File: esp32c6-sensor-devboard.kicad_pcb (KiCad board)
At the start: 4 copper layers, 90 x 50 mm, 193 parts, among them J1 Conn_01x04_Pin, J2 Micro_SD_Card_Det1, J3 Screw_Terminal_01x02, J4 USB_C_Receptacle_USB2.0_14P, J5 Screw_Terminal_01x02, J6 Screw_Terminal_01x06, J7 Screw_Terminal_01x04, J8 Conn_01x04_Pin, J9 Conn_01x03_Pin, SW1 SW_Push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

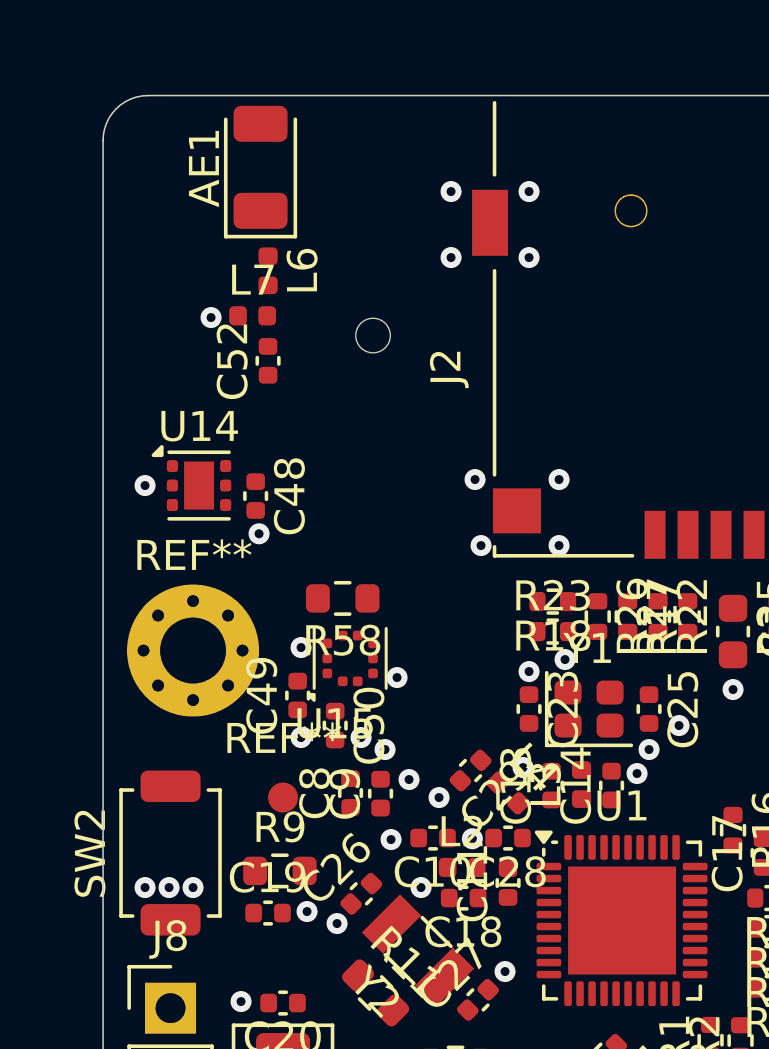
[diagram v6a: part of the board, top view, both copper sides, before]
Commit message: pcb: add rf routing
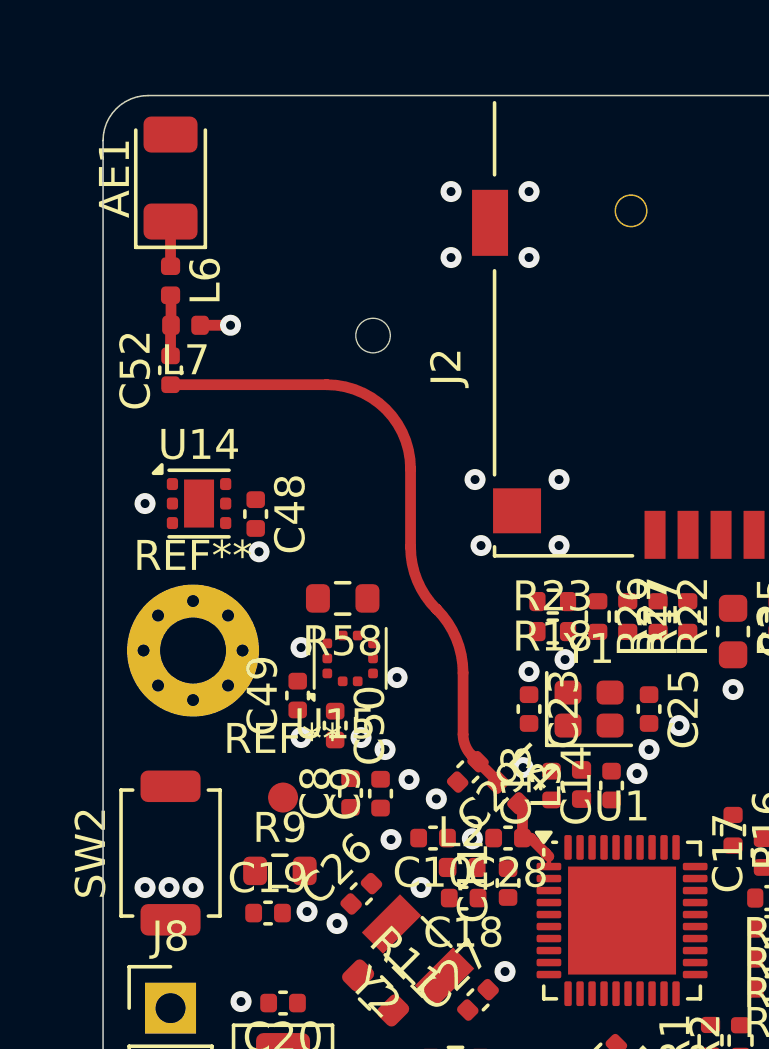
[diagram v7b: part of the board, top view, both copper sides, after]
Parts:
- moved L6 3.27 mm to (134.2, 73.2)
- moved C52 3.27 mm to (134.2, 76.2)
- moved AE1 3.02 mm to (134.2, 69.8)
- moved L7 2.26 mm to (134.8, 74.7), turned to 180 degrees
- moved C48 0.60 mm to (137.1, 81.0)
- moved U14 0.60 mm to (135.2, 80.6)
- moved C29 0.10 mm to (144.2, 89.5)
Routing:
- net /RF_TRANS: track 0.00 -> 20.8 mm
- net /RF_ESP: track 0.00 -> 2.69 mm
- net Net-(C52-Pad2): track 0.00 -> 2.03 mm
- net /RF_ANT: track 0.00 -> 1.49 mm
- net GND: track 0.00 -> 1.01 mm
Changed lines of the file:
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@@
 	(footprint "Capacitor_SMD:C_0402_1005Metric"
 		(layer "F.Cu")
-		(at 144.25 89.5 -135)
+		(at 144.159791 89.544847 -135)
 		(descr "Capacitor SMD 0402 (1005 Metric), square (rectangular) end terminal, IPC-7351 nominal, (Body size source: IPC-SM-782 page 76, https://www.pcb-3d.com/wordpress/wp-content/uploads/ipc-sm-782a_amendment_1_and_2.pdf), generated with kicad-footprint-generator")
 		(tags "capacitor")
@@
 	(footprint "Inductor_SMD:L_0402_1005Metric"
 		(layer "F.Cu")
-		(at 136.985 74.3425)
+		(at 134.75 74.6575 180)
 		(descr "Inductor SMD 0402 (1005 Metric), square (rectangular) end terminal, IPC-7351 nominal, (Body size source: http://www.tortai-tech.com/upload/download/2011102023233369053.pdf), generated with kicad-footprint-generator")
 		(tags "inductor")
@@
 		)
 		(property "JLCPCB Part #" "C77108"
-			(at 0 0 0)
+			(at 0 0 180)
 			(unlocked yes)
 			(layer "F.Fab")
@@
 		)
 		(property "Manufacturer" "Murata"
-			(at 0 0 0)
+			(at 0 0 180)
 			(unlocked yes)
 			(layer "F.Fab")
@@
 		)
 		(property "Manufacturer Part Number" "LQG15HS2N7S02D"
-			(at 0 0 0)
+			(at 0 0 180)
 			(unlocked yes)
 			(layer "F.Fab")
@@
 		(attr smd)
 		(fp_line
-			(start -0.93 -0.47)
-			(end 0.93 -0.47)
+			(start 0.93 0.47)
+			(end -0.93 0.47)
 			(stroke
 				(width 0.05)
@@
 		)
 		(fp_line
-			(start -0.93 0.47)
-			(end -0.93 -0.47)
+			(start 0.93 -0.47)
+			(end 0.93 0.47)
 			(stroke
 				(width 0.05)
@@
 		)
 		(fp_line
-			(start 0.93 -0.47)
-			(end 0.93 0.47)
+			(start -0.93 0.47)
+			(end -0.93 -0.47)
 			(stroke
 				(width 0.05)
@@
 		)
 		(fp_line
-			(start 0.93 0.47)
-			(end -0.93 0.47)
+			(start -0.93 -0.47)
+			(end 0.93 -0.47)
 			(stroke
 				(width 0.05)
@@
 		)
 		(fp_line
-			(start -0.5 -0.25)
-			(end 0.5 -0.25)
+			(start 0.5 0.25)
+			(end -0.5 0.25)
 			(stroke
 				(width 0.1)
@@
 		)
 		(fp_line
-			(start -0.5 0.25)
-			(end -0.5 -0.25)
+			(start 0.5 -0.25)
+			(end 0.5 0.25)
 			(stroke
 				(width 0.1)
@@
 		)
 		(fp_line
-			(start 0.5 -0.25)
-			(end 0.5 0.25)
+			(start -0.5 0.25)
+			(end -0.5 -0.25)
 			(stroke
 				(width 0.1)
@@
 		)
 		(fp_line
-			(start 0.5 0.25)
-			(end -0.5 0.25)
+			(start -0.5 -0.25)
+			(end 0.5 -0.25)
 			(stroke
 				(width 0.1)
@@
 		)
 		(pad "1" smd roundrect
-			(at -0.485 0)
+			(at -0.485 0 180)
 			(size 0.59 0.64)
 			(layers "F.Cu" "F.Mask" "F.Paste")
@@
 		)
 		(pad "2" smd roundrect
-			(at 0.485 0)
+			(at 0.485 0 180)
 			(size 0.59 0.64)
 			(layers "F.Cu" "F.Mask" "F.Paste")
@@
 	(footprint "Capacitor_SMD:C_0402_1005Metric"
 		(layer "F.Cu")
-		(at 137.5 75.8425 90)
+		(at 134.25 76.1575 90)
 		(descr "Capacitor SMD 0402 (1005 Metric), square (rectangular) end terminal, IPC-7351 nominal, (Body size source: IPC-SM-782 page 76, https://www.pcb-3d.com/wordpress/wp-content/uploads/ipc-sm-782a_amendment_1_and_2.pdf), generated with kicad-footprint-generator")
 		(tags "capacitor")
@@
 	(footprint "Package_SON:WSON-6-1EP_2x2mm_P0.65mm_EP1x1.6mm"
 		(layer "F.Cu")
-		(at 135.2 80)
+		(at 135.2 80.6)
 		(descr "WSON, 6 Pin (http://www.ti.com/lit/ds/symlink/tps61040.pdf#page=35), generated with kicad-footprint-generator ipc_noLead_generator.py")
 		(tags "WSON NoLead")
@@
 	(footprint "Capacitor_SMD:C_0402_1005Metric"
 		(layer "F.Cu")
-		(at 137.0875 80.35 -90)
+		(at 137.0875 80.95 -90)
 		(descr "Capacitor SMD 0402 (1005 Metric), square (rectangular) end terminal, IPC-7351 nominal, (Body size source: IPC-SM-782 page 76, https://www.pcb-3d.com/wordpress/wp-content/uploads/ipc-sm-782a_amendment_1_and_2.pdf), generated with kicad-footprint-generator")
 		(tags "capacitor")
@@
 	(footprint "Inductor_SMD:L_0402_1005Metric"
 		(layer "F.Cu")
-		(at 137.5 72.8425 -90)
+		(at 134.25 73.1725 -90)
 		(descr "Inductor SMD 0402 (1005 Metric), square (rectangular) end terminal, IPC-7351 nominal, (Body size source: http://www.tortai-tech.com/upload/download/2011102023233369053.pdf), generated with kicad-footprint-generator")
 		(tags "inductor")
@@
 	(footprint "RF_Antenna:Johanson_2450AT18x100"
 		(layer "F.Cu")
-		(at 137.25 69.3925 90)
+		(at 134.25 69.75 90)
 		(descr "Johanson 2450AT43F0100 SMD antenna 2400-2500Mhz, -0.5dBi, https://www.johansontechnology.com/datasheets/2450AT18A100/2450AT18A100.pdf")
 		(tags "antenna")
@@
 		(layer "Edge.Cuts")
 	)
+	(segment
+		(start 134.25 72.6875)
+		(end 134.25 71.2)
+		(width 0.359)
+		(layer "F.Cu")
+		(net 1)
+	)
+	(segment
+		(start 135.235 74.6575)
+		(end 136.25 74.6575)
+		(width 0.359)
+		(layer "F.Cu")
+		(net 2)
+	)
 	(via
-		(at 133.4 80)
+		(at 133.4 80.6)
 		(size 0.7)
 		(drill 0.3)
@@
 	)
 	(via
-		(at 143.2 90.4)
+		(at 143.109791 90.444847)
 		(size 0.7)
 		(drill 0.3)
@@
 	)
 	(via
+		(at 136.25 74.6575)
+		(size 0.7)
+		(drill 0.3)
+		(layers "F.Cu" "B.Cu")
+		(free yes)
+		(net 2)
+	)
+	(via
 		(at 180.4 83.6)
 		(size 0.7)
@@
 	)
 	(via
-		(at 135.6 74.4)
-		(size 0.7)
-		(drill 0.3)
-		(layers "F.Cu" "B.Cu")
-		(free yes)
-		(net 2)
-	)
-	(via
 		(at 141.8 107.2)
 		(size 0.7)
@@
 	)
 	(via
-		(at 137.2 81.6075)
+		(at 137.2 82.2075)
 		(size 0.7)
 		(drill 0.3)
@@
 		(net 51)
 	)
+	(segment
+		(start 145.98 91.75)
+		(end 145.98 90.73)
+		(width 0.359)
+		(layer "F.Cu")
+		(net 121)
+	)
+	(segment
+		(start 146.8625 92.7)
+		(end 146.8625 92.3625)
+		(width 0.15)
+		(layer "F.Cu")
+		(net 121)
+	)
+	(segment
+		(start 146.75 92.25)
+		(end 146.25 91.75)
+		(width 0.359)
+		(layer "F.Cu")
+		(net 121)
+	)
+	(segment
+		(start 146.8625 92.3625)
+		(end 146.75 92.25)
+		(width 0.359)
+		(layer "F.Cu")
+		(net 121)
+	)
+	(segment
+		(start 146.25 91.75)
+		(end 145.98 91.75)
+		(width 0.359)
+		(layer "F.Cu")
+		(net 121)
+	)
+	(segment
+		(start 145.98 90.73)
+		(end 145.842947 90.592947)
+		(width 0.359)
+		(layer "F.Cu")
+		(net 121)
+	)
+	(segment
+		(start 143.12132 84.12132)
+		(end 143.110548 84.12132)
+		(width 0.359)
+		(layer "F.Cu")
+		(net 122)
+	)
+	(segment
+		(start 144.499202 89.205436)
+		(end 144.292893 88.999127)
+		(width 0.359)
+		(layer "F.Cu")
+		(net 122)
+	)
+	(segment
+		(start 145.157053 89.863287)
+		(end 144.499202 89.205436)
+		(width 0.359)
+		(layer "F.Cu")
+		(net 122)
+	)
+	(segment
+		(start 142.25 82.043895)
+		(end 142.25 79.437327)
+		(width 0.359)
+		(layer "F.Cu")
+		(net 122)
+	)
+	(segment
+		(start 145.157053 89.907053)
+		(end 145.157053 89.863287)
+		(width 0.359)
+		(layer "F.Cu")
+		(net 122)
+	)
+	(segment
+		(start 144 88.29202)
+		(end 144 86.242616)
+		(width 0.359)
+		(layer "F.Cu")
+		(net 122)
+	)
+	(segment
+		(start 139.450173 76.6375)
+		(end 134.25 76.6375)
+		(width 0.359)
+		(layer "F.Cu")
+		(net 122)
+	)
+	(arc
+		(start 142.25 79.437327)
+		(mid 141.42995 77.45755)
+		(end 139.450173 76.6375)
+		(width 0.359)
+		(layer "F.Cu")
+		(net 122)
+	)
+	(arc
+		(start 144 86.242616)
+		(mid 143.771648 85.0946)
+		(end 143.12132 84.12132)
+		(width 0.359)
+		(layer "F.Cu")
+		(net 122)
+	)
+	(arc
+		(start 143.110548 84.12132)
+		(mid 142.473626 83.168142)
+		(end 142.25 82.043895)
+		(width 0.359)
+		(layer "F.Cu")
+		(net 122)
+	)
+	(arc
+		(start 144.292893 88.999127)
+		(mid 144.07612 88.674703)
+		(end 144 88.29202)
+		(width 0.359)
+		(layer "F.Cu")
+		(net 122)
+	)
+	(segment
+		(start 134.265 74.6575)
+		(end 134.265 73.6725)
+		(width 0.359)
+		(layer "F.Cu")
+		(net 123)
+	)
+	(segment
+		(start 134.265 73.6725)
+		(end 134.25 73.6575)
+		(width 0.359)
+		(layer "F.Cu")
+		(net 123)
+	)
+	(segment
+		(start 134.25 75.6775)
+		(end 134.25 74.6725)
+		(width 0.359)
+		(layer "F.Cu")
+		(net 123)
+	)
+	(segment
+		(start 134.25 74.6725)
+		(end 134.265 74.6575)
+		(width 0.359)
+		(layer "F.Cu")
+		(net 123)
+	)
 	(zone
 		(net 100)
@@
 			)
 		)
+	)
+	(zone
+		(net 0)
+		(net_name "")
+		(layers "F.Cu" "B.Cu" "In1.Cu" "In2.Cu")
+		(hatch edge 0.5)
+		(connect_pads
+			(clearance 0)
+		)
+		(min_thickness 0.25)
+		(filled_areas_thickness no)
+		(keepout
+			(tracks allowed)
+			(vias allowed)
+			(pads allowed)
+			(copperpour not_allowed)
+			(footprints allowed)
+		)
+		(placement
+			(enabled no)
+			(sheetname "")
+		)
+		(fill
+			(thermal_gap 0.5)
+			(thermal_bridge_width 0.5)
+		)
+		(polygon
+			(pts
+				(xy 132 67) (xy 142.5 67) (xy 142.5 74.25) (xy 132 74.25)
+			)
+		)

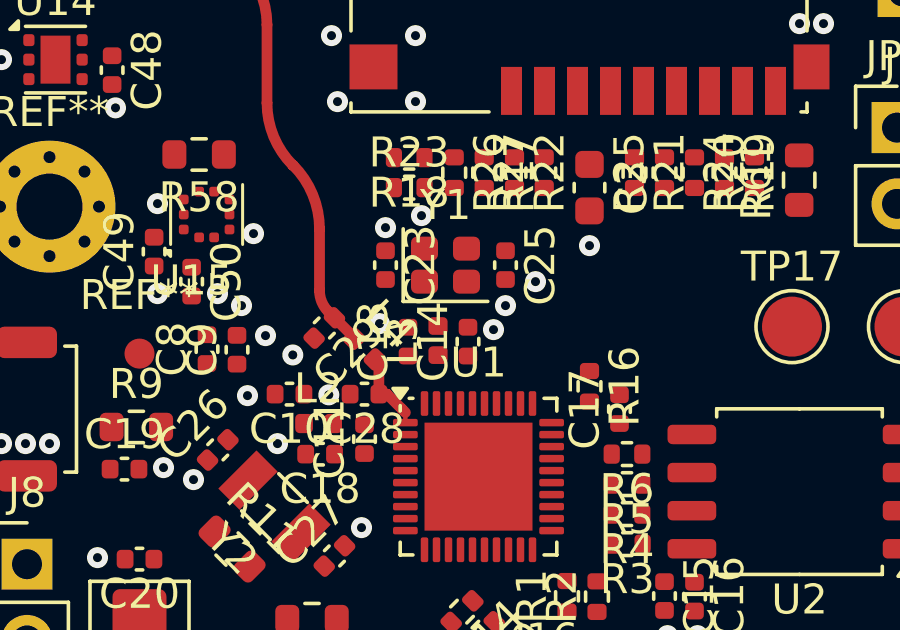
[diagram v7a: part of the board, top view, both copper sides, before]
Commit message: pcb: add HSE routing
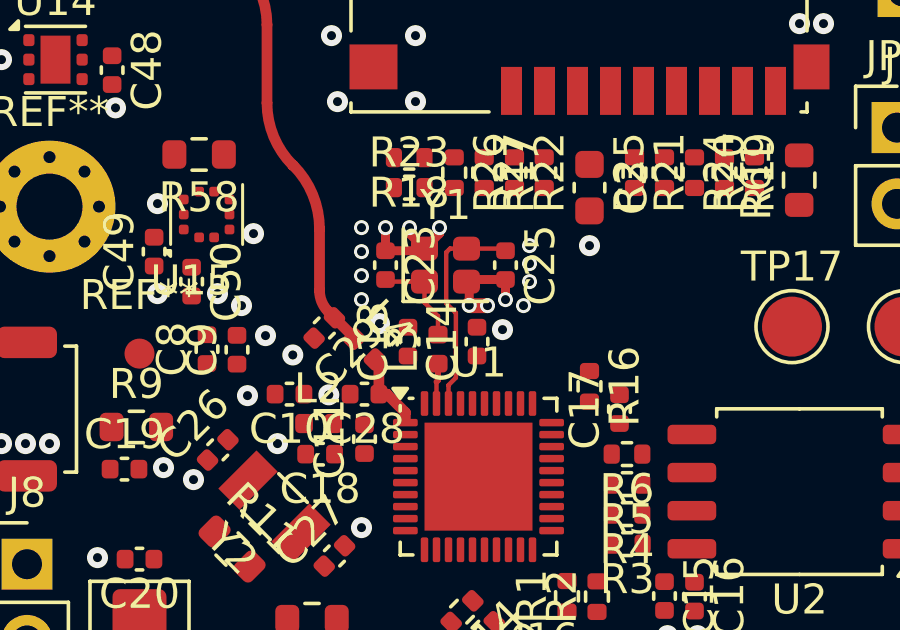
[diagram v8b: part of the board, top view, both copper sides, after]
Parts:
- moved C14 0.30 mm to (149.2, 90.0)
- moved L3 0.28 mm to (147.9, 90.2)
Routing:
- net GND: track 1.01 -> 8.60 mm, vias 102 -> 112
- net /XTAL_N: track 0.00 -> 7.33 mm
- net /XTAL_PL: track 0.00 -> 3.28 mm
- net /XTAL_P: track 0.00 -> 1.35 mm
